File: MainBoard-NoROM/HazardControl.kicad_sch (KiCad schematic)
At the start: 6 parts, among them U12 ATF22V10C-7PX, U13 ATF22V10C-7PX

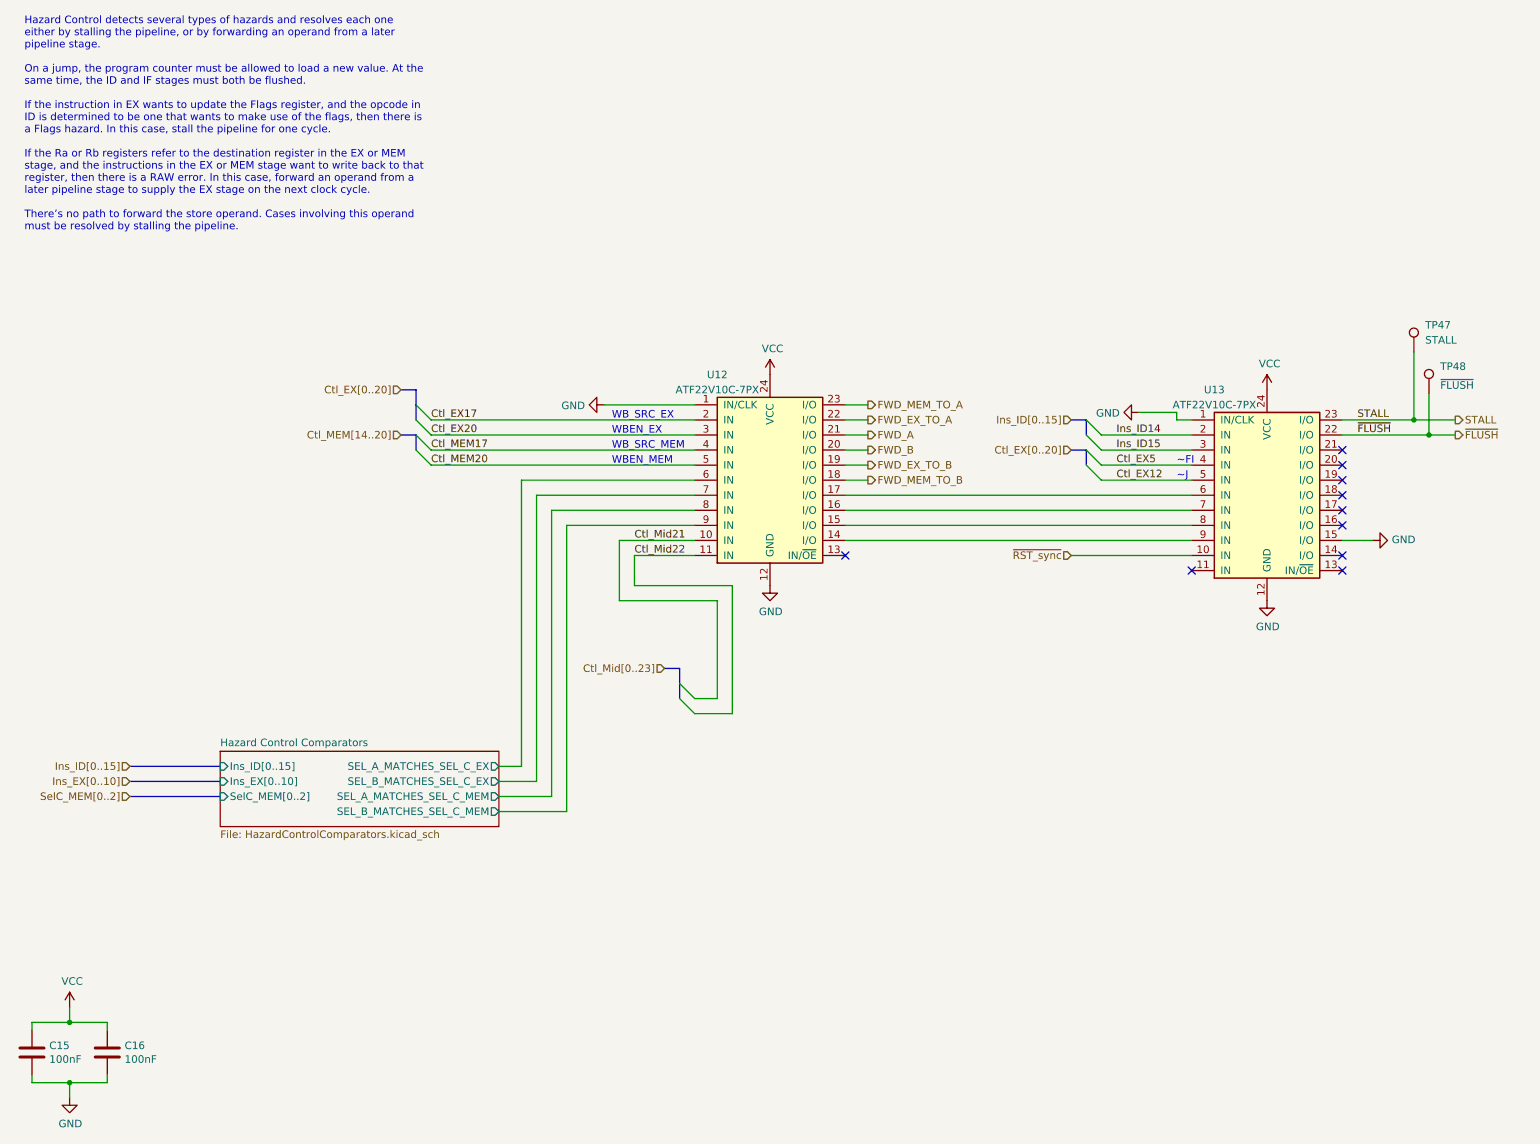
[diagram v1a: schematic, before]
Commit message: Update schematics for the MainBoard to include the ControleModule fix from 704c0dce
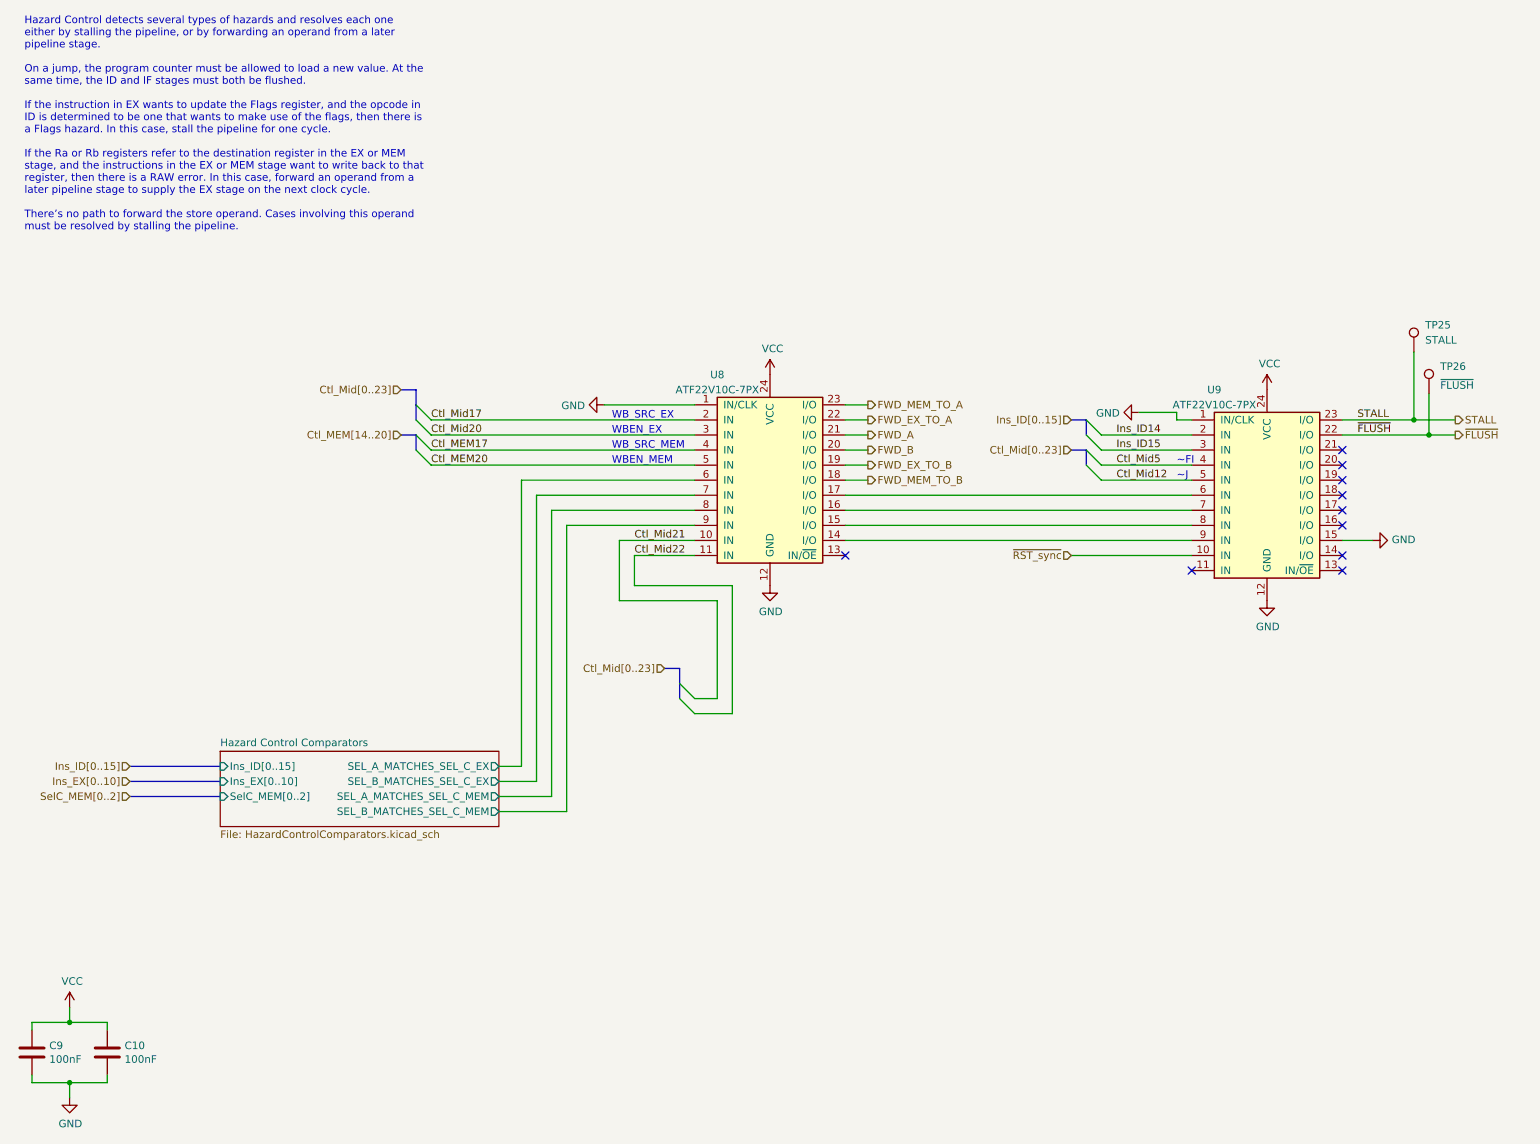
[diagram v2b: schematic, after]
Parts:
- renumbered C16 to C10, C15 to C9, TP47 to TP25, TP48 to TP26, U12 to U8, U13 to U9
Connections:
- net Ctl_EX12 renamed Ctl_Mid12
- net Ctl_EX17 renamed Ctl_Mid17
- net Ctl_EX20 renamed Ctl_Mid20
- net Ctl_EX5 renamed Ctl_Mid5
